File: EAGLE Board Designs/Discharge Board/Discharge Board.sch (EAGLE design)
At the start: 7 parts, among them K1 RELAY_SPST_NC_POLARIZED_D_24

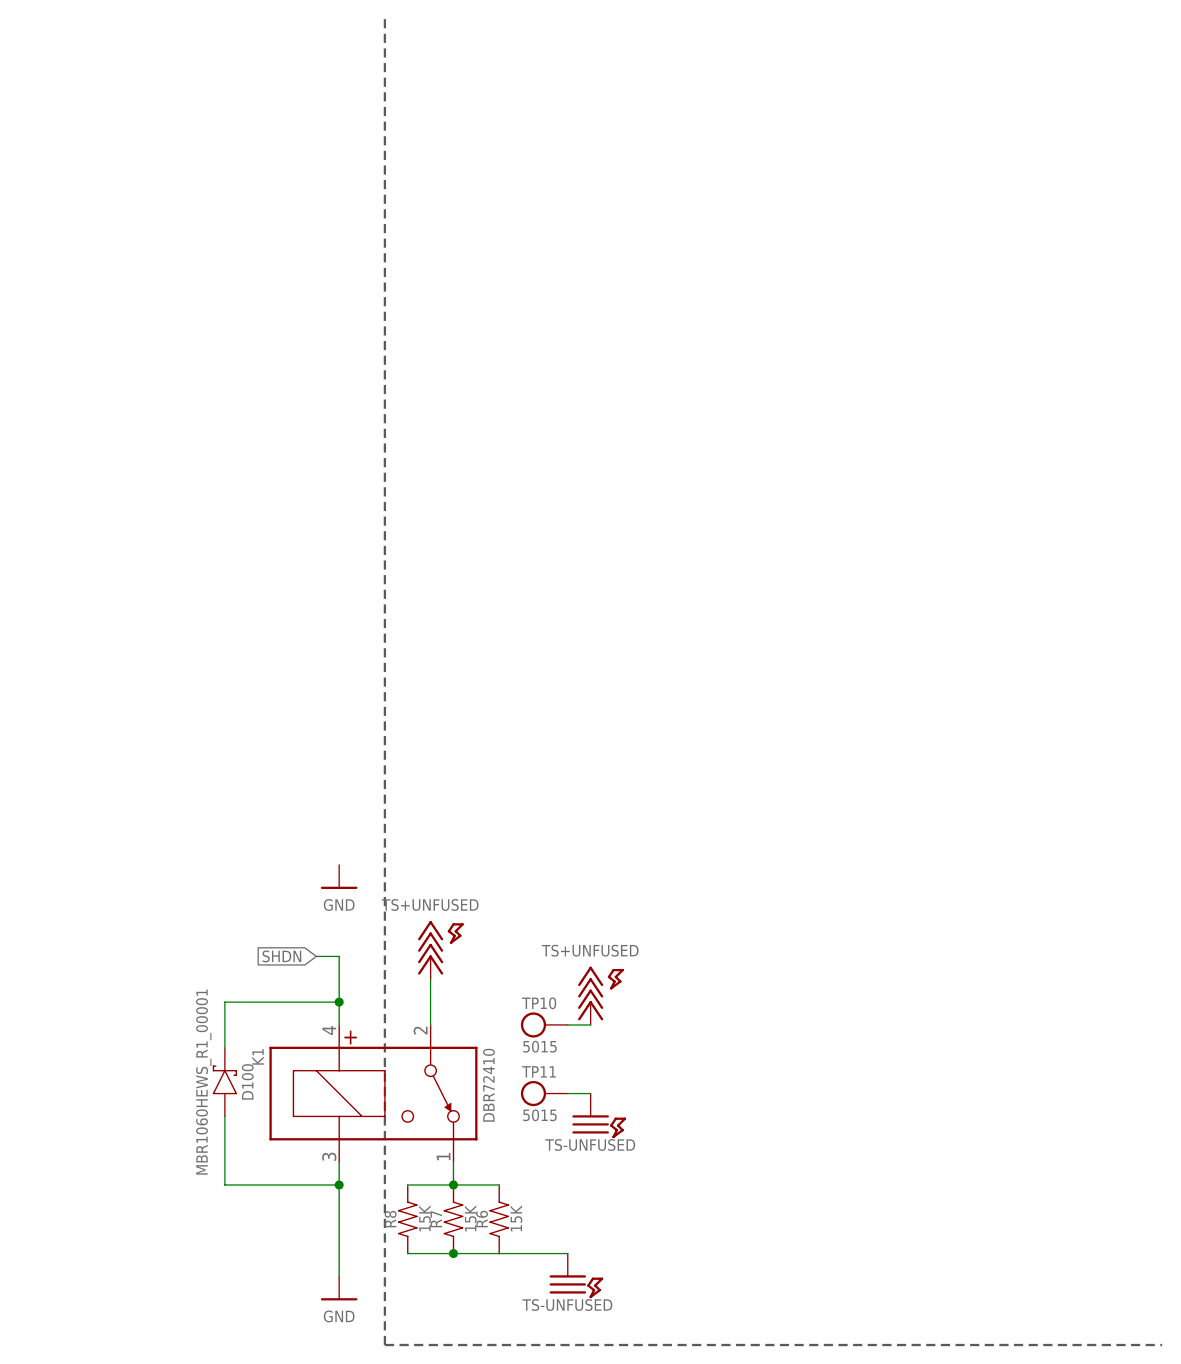
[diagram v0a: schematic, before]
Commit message: Update Discharge Board.sch
Added 1 Molex microfit right angle single row connector
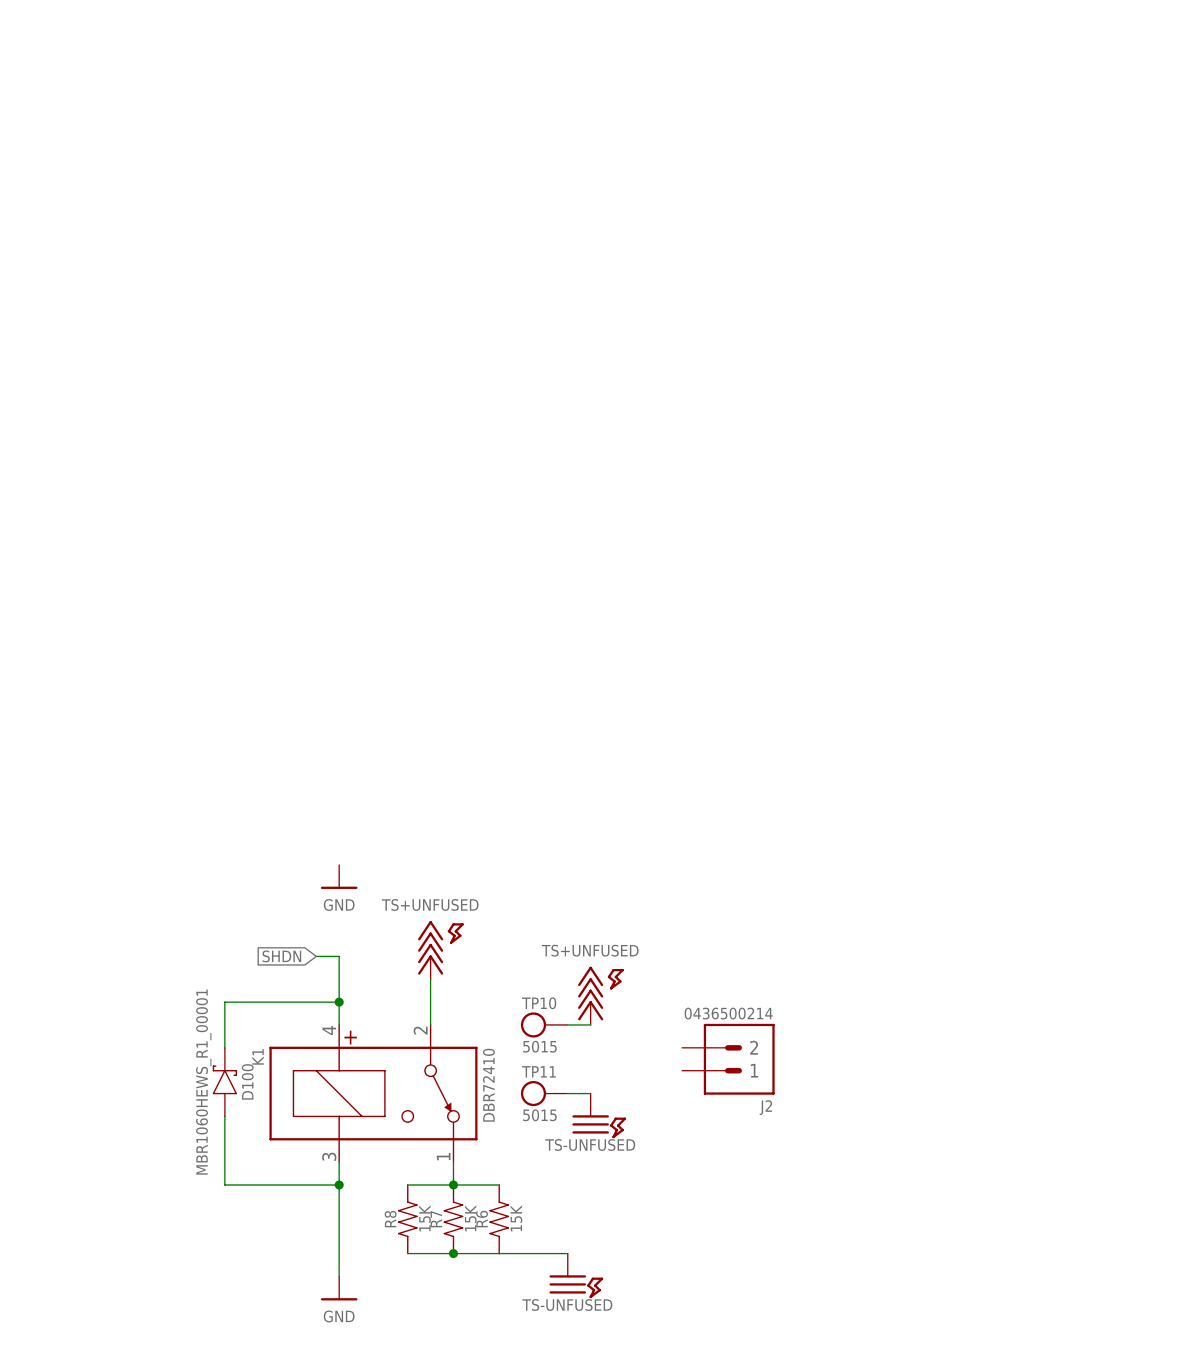
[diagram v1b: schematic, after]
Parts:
- added J2: CONNECTOR-2_MICROFIT_SMD_RIGHTANGLE_02_SINGLE_BLACK, HyTechDevices:CONNECTOR-2_MICROFIT_SMD_RIGHTANGLE_02_SINGLE_BLACK
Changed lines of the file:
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@@
 <part name="R8" library="HyTechDevices" deviceset="RESISTOR_?_*" device="B20" technology="15K"/>
 <part name="K1" library="HyTechDevices" deviceset="RELAY_SPST_NC_POLARIZED_?*" device="D_" technology="24"/>
+<part name="J2" library="HyTechDevices" deviceset="CONNECTOR-2_?_*" device="MICROFIT_SMD_RIGHTANGLE_02_SINGLE" technology="BLACK"/>
 </parts>
 <sheets>
 <sheet>
 <plain>
-<wire x1="27.94" y1="149.86" x2="27.94" y2="2.54" width="0.254" layer="97" style="longdash"/>
-<wire x1="27.94" y1="2.54" x2="114.3" y2="2.54" width="0.254" layer="97" style="longdash"/>
 </plain>
 <instances>
@@
 <attribute name="NAME" x="14.478" y="35.56" size="1.27" layer="95" rot="MR270"/>
 </instance>
+<instance part="J2" gate="G$1" x="71.12" y="30.48" smashed="yes" rot="R180">
+<attribute name="MPN" x="71.12" y="38.735" size="1.27" layer="96" rot="R180" align="top-left"/>
+<attribute name="NAME" x="71.12" y="29.718" size="1.27" layer="95" rot="R180"/>
+</instance>
 </instances>

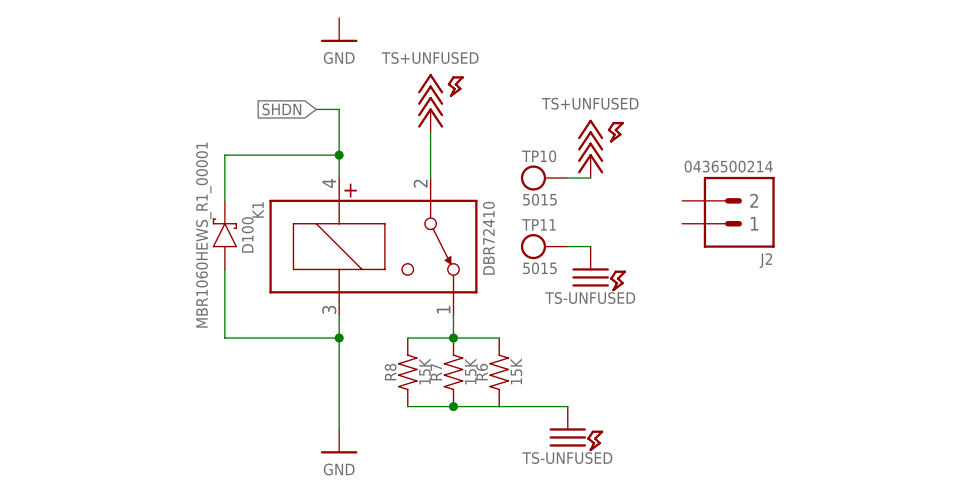
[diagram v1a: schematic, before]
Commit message: Finished adding 2 2pin molex connectors in sch. Created brd
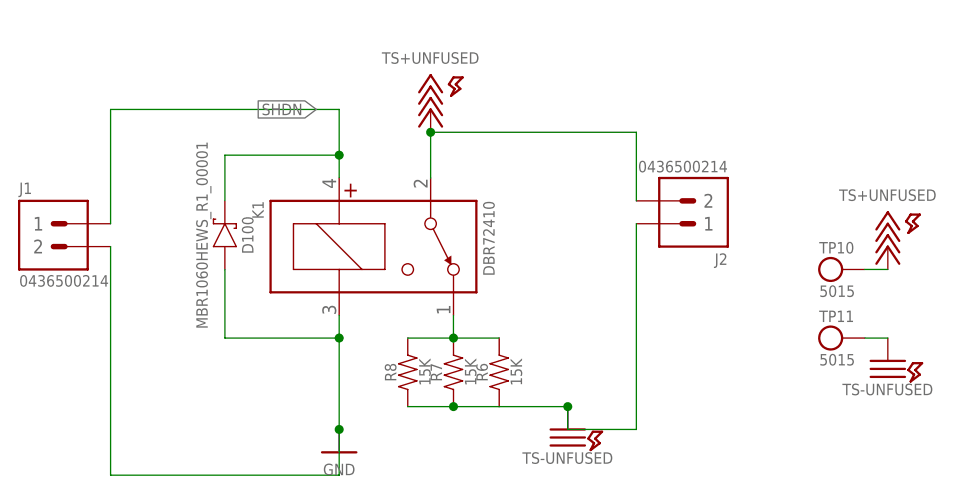
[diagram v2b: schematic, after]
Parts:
- added J1: CONNECTOR-2_MICROFIT_SMD_RIGHTANGLE_02_SINGLE_BLACK, HyTechDevices:CONNECTOR-2_MICROFIT_SMD_RIGHTANGLE_02_SINGLE_BLACK
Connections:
- net GND: now also J1.2
- net N$5: now also J2.1
- net SHDN: now also J1.1
- net TS+UNFUSED: now also J2.2
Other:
- moved on the sheet: J2, TP10, TP11
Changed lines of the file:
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@@
 <parts>
 <part name="D100" library="HyTechDevices" deviceset="SCHOTTKY_?_*" device="SOD323" technology="60V" value="SCHOTTKY_SOD323_60V"/>
-<part name="P33" library="HyTechSupplies" deviceset="GND" device=""/>
 <part name="P36" library="HyTechSupplies" deviceset="TS+UNFUSED" device=""/>
 <part name="P2" library="HyTechSupplies" deviceset="GND" device=""/>
@@
 <part name="K1" library="HyTechDevices" deviceset="RELAY_SPST_NC_POLARIZED_?*" device="D_" technology="24"/>
 <part name="J2" library="HyTechDevices" deviceset="CONNECTOR-2_?_*" device="MICROFIT_SMD_RIGHTANGLE_02_SINGLE" technology="BLACK"/>
+<part name="J1" library="HyTechDevices" deviceset="CONNECTOR-2_?_*" device="MICROFIT_SMD_RIGHTANGLE_02_SINGLE" technology="BLACK"/>
 </parts>
 <sheets>
@@
 <attribute name="MPN" x="8.255" y="31.75" size="1.27" layer="96" rot="MR90" align="top-center"/>
 </instance>
-<instance part="P33" gate="1" x="22.86" y="53.34" smashed="yes" rot="MR0">
-<attribute name="VALUE" x="22.86" y="52.07" size="1.27" layer="96" rot="MR0" align="top-center"/>
-</instance>
 <instance part="P36" gate="G$1" x="33.02" y="45.72" smashed="yes">
 <attribute name="VALUE" x="33.02" y="50.8" size="1.27" layer="96" align="bottom-center"/>
@@
 <attribute name="VALUE" x="22.86" y="6.35" size="1.27" layer="96" rot="MR0" align="top-center"/>
 </instance>
-<instance part="TP11" gate="G$1" x="45.72" y="30.48" smashed="yes">
-<attribute name="NAME" x="43.18" y="32.258" size="1.27" layer="95"/>
-<attribute name="MPN" x="43.18" y="28.702" size="1.27" layer="95" align="top-left"/>
+<instance part="TP11" gate="G$1" x="78.74" y="20.32" smashed="yes">
+<attribute name="NAME" x="76.2" y="22.098" size="1.27" layer="95"/>
+<attribute name="MPN" x="76.2" y="18.542" size="1.27" layer="95" align="top-left"/>
 </instance>
-<instance part="TP10" gate="G$1" x="45.72" y="38.1" smashed="yes">
-<attribute name="NAME" x="43.18" y="39.878" size="1.27" layer="95"/>
-<attribute name="MPN" x="43.18" y="36.322" size="1.27" layer="95" align="top-left"/>
+<instance part="TP10" gate="G$1" x="78.74" y="27.94" smashed="yes">
+<attribute name="NAME" x="76.2" y="29.718" size="1.27" layer="95"/>
+<attribute name="MPN" x="76.2" y="26.162" size="1.27" layer="95" align="top-left"/>
 </instance>
-<instance part="P11" gate="G$1" x="50.8" y="40.64" smashed="yes">
-<attribute name="VALUE" x="50.8" y="45.72" size="1.27" layer="96" align="bottom-center"/>
+<instance part="P11" gate="G$1" x="83.82" y="30.48" smashed="yes">
+<attribute name="VALUE" x="83.82" y="35.56" size="1.27" layer="96" align="bottom-center"/>
 </instance>
 <instance part="P12" gate="G$1" x="48.26" y="10.16" smashed="yes">
 <attribute name="VALUE" x="48.26" y="7.62" size="1.27" layer="96" align="top-center"/>
 </instance>
-<instance part="P15" gate="G$1" x="50.8" y="27.94" smashed="yes">
-<attribute name="VALUE" x="50.8" y="25.4" size="1.27" layer="96" align="top-center"/>
+<instance part="P15" gate="G$1" x="83.82" y="17.78" smashed="yes">
+<attribute name="VALUE" x="83.82" y="15.24" size="1.27" layer="96" align="top-center"/>
 </instance>
 <instance part="R6" gate="G$1" x="40.64" y="17.78" smashed="yes" rot="R90">
@@
 <attribute name="NAME" x="14.478" y="35.56" size="1.27" layer="95" rot="MR270"/>
 </instance>
-<instance part="J2" gate="G$1" x="71.12" y="30.48" smashed="yes" rot="R180">
-<attribute name="MPN" x="71.12" y="38.735" size="1.27" layer="96" rot="R180" align="top-left"/>
-<attribute name="NAME" x="71.12" y="29.718" size="1.27" layer="95" rot="R180"/>
+<instance part="J2" gate="G$1" x="66.04" y="30.48" smashed="yes" rot="R180">
+<attribute name="MPN" x="66.04" y="38.735" size="1.27" layer="96" rot="R180" align="top-left"/>
+<attribute name="NAME" x="66.04" y="29.718" size="1.27" layer="95" rot="R180"/>
+</instance>
+<instance part="J1" gate="G$1" x="-12.7" y="35.56" smashed="yes">
+<attribute name="MPN" x="-12.7" y="27.305" size="1.27" layer="96" align="top-left"/>
+<attribute name="NAME" x="-12.7" y="36.322" size="1.27" layer="95"/>
 </instance>
 </instances>
@@
 <junction x="22.86" y="20.32"/>
 <pinref part="K1" gate="G$1" pin="COIL-"/>
+<pinref part="J1" gate="G$1" pin="2"/>
+<wire x1="-2.54" y1="30.48" x2="-2.54" y2="5.08" width="0.1524" layer="91"/>
+<wire x1="-2.54" y1="5.08" x2="22.86" y2="5.08" width="0.1524" layer="91"/>
+<wire x1="22.86" y1="5.08" x2="22.86" y2="10.16" width="0.1524" layer="91"/>
+<junction x="22.86" y="10.16"/>
 </segment>
 </net>
@@
 <wire x1="22.86" y1="45.72" x2="20.32" y2="45.72" width="0.1524" layer="91"/>
 <pinref part="K1" gate="G$1" pin="COIL+"/>
+<pinref part="J1" gate="G$1" pin="1"/>
+<wire x1="-2.54" y1="33.02" x2="-2.54" y2="45.72" width="0.1524" layer="91"/>
+<wire x1="-2.54" y1="45.72" x2="20.32" y2="45.72" width="0.1524" layer="91"/>
 </segment>
 </net>
@@
 <wire x1="33.02" y1="43.18" x2="33.02" y2="38.1" width="0.6096" layer="91"/>
 <pinref part="K1" gate="G$1" pin="CONTACT1"/>
+<pinref part="J2" gate="G$1" pin="2"/>
+<wire x1="55.88" y1="35.56" x2="55.88" y2="43.18" width="0.1524" layer="91"/>
+<wire x1="55.88" y1="43.18" x2="33.02" y2="43.18" width="0.1524" layer="91"/>
+<junction x="33.02" y="43.18"/>
 </segment>
 <segment>
 <pinref part="TP10" gate="G$1" pin="1"/>
-<wire x1="48.26" y1="38.1" x2="50.8" y2="38.1" width="0.6096" layer="91"/>
+<wire x1="81.28" y1="27.94" x2="83.82" y2="27.94" width="0.6096" layer="91"/>
 <pinref part="P11" gate="G$1" pin="TS+UNFUSED"/>
 </segment>
@@
 <segment>
 <pinref part="TP11" gate="G$1" pin="1"/>
-<wire x1="48.26" y1="30.48" x2="50.8" y2="30.48" width="0.6096" layer="91"/>
+<wire x1="81.28" y1="20.32" x2="83.82" y2="20.32" width="0.6096" layer="91"/>
 <pinref part="P15" gate="G$1" pin="TS-UNFUSED"/>
 </segment>
@@
 <pinref part="P12" gate="G$1" pin="TS-UNFUSED"/>
 <wire x1="40.64" y1="12.7" x2="48.26" y2="12.7" width="0.6096" layer="91"/>
+<pinref part="J2" gate="G$1" pin="1"/>
+<wire x1="55.88" y1="33.02" x2="55.88" y2="10.16" width="0.1524" layer="91"/>
+<wire x1="55.88" y1="10.16" x2="48.26" y2="10.16" width="0.1524" layer="91"/>
+<wire x1="48.26" y1="10.16" x2="48.26" y2="12.7" width="0.1524" layer="91"/>
+<junction x="48.26" y="12.7"/>
 </segment>
 </net>

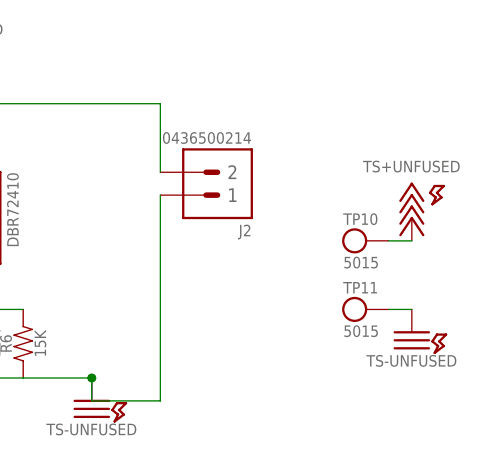
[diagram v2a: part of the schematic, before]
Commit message: Correct sch->board
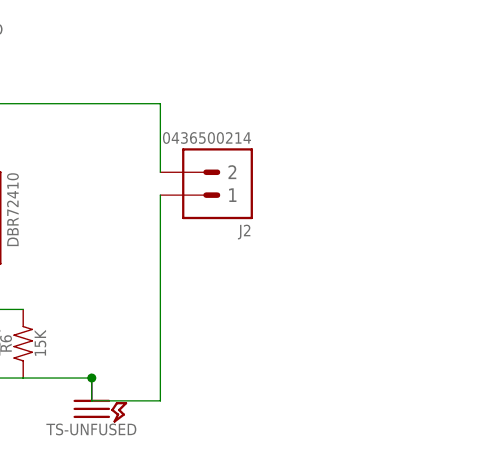
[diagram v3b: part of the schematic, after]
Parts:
- removed TP10, TP11: TEST_POINT, HyTechDevices:TEST_POINT
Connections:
- removed net TS-UNFUSED: TP11.1
- net TS+UNFUSED: no longer TP10.1
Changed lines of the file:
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@@
 <part name="P36" library="HyTechSupplies" deviceset="TS+UNFUSED" device=""/>
 <part name="P2" library="HyTechSupplies" deviceset="GND" device=""/>
-<part name="TP11" library="HyTechDevices" deviceset="TEST_POINT" device=""/>
-<part name="TP10" library="HyTechDevices" deviceset="TEST_POINT" device=""/>
-<part name="P11" library="HyTechSupplies" deviceset="TS+UNFUSED" device=""/>
 <part name="P12" library="HyTechSupplies" deviceset="TS-UNFUSED" device=""/>
-<part name="P15" library="HyTechSupplies" deviceset="TS-UNFUSED" device=""/>
 <part name="R6" library="HyTechDevices" deviceset="RESISTOR_?_*" device="B20" technology="15K"/>
 <part name="R7" library="HyTechDevices" deviceset="RESISTOR_?_*" device="B20" technology="15K"/>
@@
 <attribute name="VALUE" x="22.86" y="6.35" size="1.27" layer="96" rot="MR0" align="top-center"/>
 </instance>
-<instance part="TP11" gate="G$1" x="78.74" y="20.32" smashed="yes">
-<attribute name="NAME" x="76.2" y="22.098" size="1.27" layer="95"/>
-<attribute name="MPN" x="76.2" y="18.542" size="1.27" layer="95" align="top-left"/>
-</instance>
-<instance part="TP10" gate="G$1" x="78.74" y="27.94" smashed="yes">
-<attribute name="NAME" x="76.2" y="29.718" size="1.27" layer="95"/>
-<attribute name="MPN" x="76.2" y="26.162" size="1.27" layer="95" align="top-left"/>
-</instance>
-<instance part="P11" gate="G$1" x="83.82" y="30.48" smashed="yes">
-<attribute name="VALUE" x="83.82" y="35.56" size="1.27" layer="96" align="bottom-center"/>
-</instance>
 <instance part="P12" gate="G$1" x="48.26" y="10.16" smashed="yes">
 <attribute name="VALUE" x="48.26" y="7.62" size="1.27" layer="96" align="top-center"/>
-</instance>
-<instance part="P15" gate="G$1" x="83.82" y="17.78" smashed="yes">
-<attribute name="VALUE" x="83.82" y="15.24" size="1.27" layer="96" align="top-center"/>
 </instance>
 <instance part="R6" gate="G$1" x="40.64" y="17.78" smashed="yes" rot="R90">
@@
 <junction x="33.02" y="43.18"/>
 </segment>
-<segment>
-<pinref part="TP10" gate="G$1" pin="1"/>
-<wire x1="81.28" y1="27.94" x2="83.82" y2="27.94" width="0.6096" layer="91"/>
-<pinref part="P11" gate="G$1" pin="TS+UNFUSED"/>
-</segment>
 </net>
 <net name="N$51" class="0">
@@
 </segment>
 </net>
-<net name="TS-UNFUSED" class="0">
-<segment>
-<pinref part="TP11" gate="G$1" pin="1"/>
-<wire x1="81.28" y1="20.32" x2="83.82" y2="20.32" width="0.6096" layer="91"/>
-<pinref part="P15" gate="G$1" pin="TS-UNFUSED"/>
-</segment>
-</net>

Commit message: made components fit better?
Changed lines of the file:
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@@
 <pinref part="K1" gate="G$1" pin="COIL-"/>
 <pinref part="J1" gate="G$1" pin="2"/>
-<wire x1="-2.54" y1="30.48" x2="-2.54" y2="5.08" width="0.1524" layer="91"/>
-<wire x1="-2.54" y1="5.08" x2="22.86" y2="5.08" width="0.1524" layer="91"/>
-<wire x1="22.86" y1="5.08" x2="22.86" y2="10.16" width="0.1524" layer="91"/>
+<wire x1="-2.54" y1="30.48" x2="-2.54" y2="12.7" width="0.1524" layer="91"/>
+<wire x1="-2.54" y1="12.7" x2="22.86" y2="12.7" width="0.1524" layer="91"/>
+<wire x1="22.86" y1="12.7" x2="22.86" y2="10.16" width="0.1524" layer="91"/>
 <junction x="22.86" y="10.16"/>
 </segment>
@@
 <wire x1="22.86" y1="40.64" x2="22.86" y2="38.1" width="0.1524" layer="91"/>
 <junction x="22.86" y="40.64"/>
-<label x="20.32" y="45.72" size="1.27" layer="95" rot="MR0" xref="yes"/>
+<label x="22.86" y="45.72" size="1.27" layer="95" rot="MR180" xref="yes"/>
 <wire x1="22.86" y1="40.64" x2="22.86" y2="45.72" width="0.1524" layer="91"/>
-<wire x1="22.86" y1="45.72" x2="20.32" y2="45.72" width="0.1524" layer="91"/>
 <pinref part="K1" gate="G$1" pin="COIL+"/>
 <pinref part="J1" gate="G$1" pin="1"/>
 <wire x1="-2.54" y1="33.02" x2="-2.54" y2="45.72" width="0.1524" layer="91"/>
-<wire x1="-2.54" y1="45.72" x2="20.32" y2="45.72" width="0.1524" layer="91"/>
+<wire x1="-2.54" y1="45.72" x2="22.86" y2="45.72" width="0.1524" layer="91"/>
 </segment>
 </net>
@@
 <pinref part="K1" gate="G$1" pin="CONTACT1"/>
 <pinref part="J2" gate="G$1" pin="2"/>
-<wire x1="55.88" y1="35.56" x2="55.88" y2="43.18" width="0.1524" layer="91"/>
-<wire x1="55.88" y1="43.18" x2="33.02" y2="43.18" width="0.1524" layer="91"/>
+<wire x1="55.88" y1="35.56" x2="55.88" y2="43.18" width="0.6096" layer="91"/>
+<wire x1="55.88" y1="43.18" x2="33.02" y2="43.18" width="0.6096" layer="91"/>
 <junction x="33.02" y="43.18"/>
 </segment>
@@
 <wire x1="40.64" y1="12.7" x2="48.26" y2="12.7" width="0.6096" layer="91"/>
 <pinref part="J2" gate="G$1" pin="1"/>
-<wire x1="55.88" y1="33.02" x2="55.88" y2="10.16" width="0.1524" layer="91"/>
-<wire x1="55.88" y1="10.16" x2="48.26" y2="10.16" width="0.1524" layer="91"/>
-<wire x1="48.26" y1="10.16" x2="48.26" y2="12.7" width="0.1524" layer="91"/>
+<wire x1="55.88" y1="33.02" x2="55.88" y2="12.7" width="0.6096" layer="91"/>
+<wire x1="55.88" y1="12.7" x2="48.26" y2="12.7" width="0.6096" layer="91"/>
 <junction x="48.26" y="12.7"/>
 </segment>
